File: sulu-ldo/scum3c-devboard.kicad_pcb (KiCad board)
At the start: 2 copper layers, 41.7 x 36.1 mm, 55 parts, among them J1 Conn_02x11_Odd_Even, J10 through_hole, J11 through_hole, J12 through_hole, J13 through_hole, J14 through_hole, J15 through_hole, J16 through_hole, J17 through_hole, J18 through_hole, J19 through_hole, J2 Conn_02x10_Odd_Even, J20 through_hole, J21 through_hole, J3 Conn_02x05_Odd_Even, J4 Conn_01x01_Male, J5 through_hole, J6 through_hole, J7 through_hole, J8 through_hole, J9 through_hole, U1 scum3, U2 S-85S1AB18-I6T1U, U3 S-85S1AB11-I6T1U, U9AB1 ICM-20948

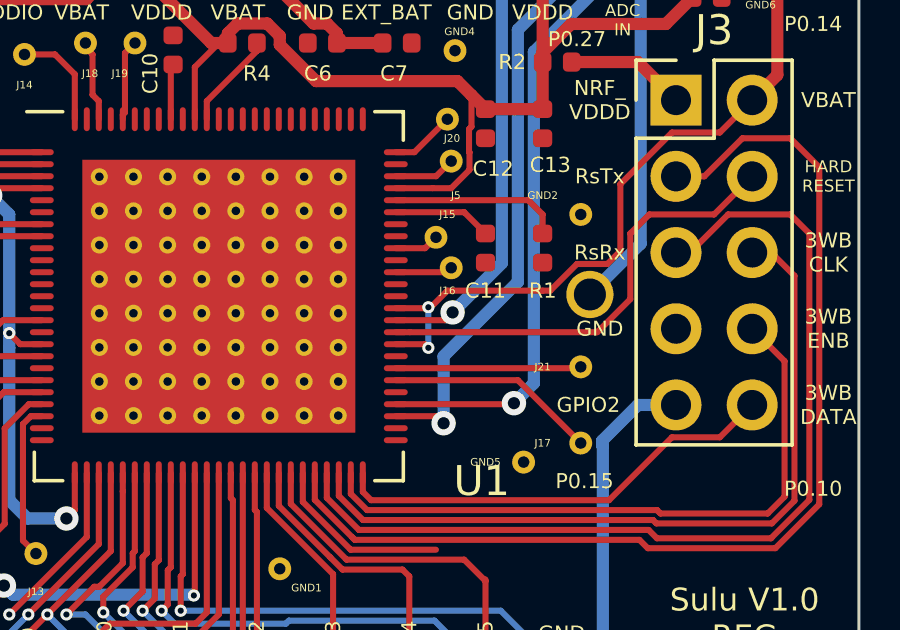
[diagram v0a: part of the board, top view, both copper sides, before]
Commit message: updated ldo with 3d model from reg
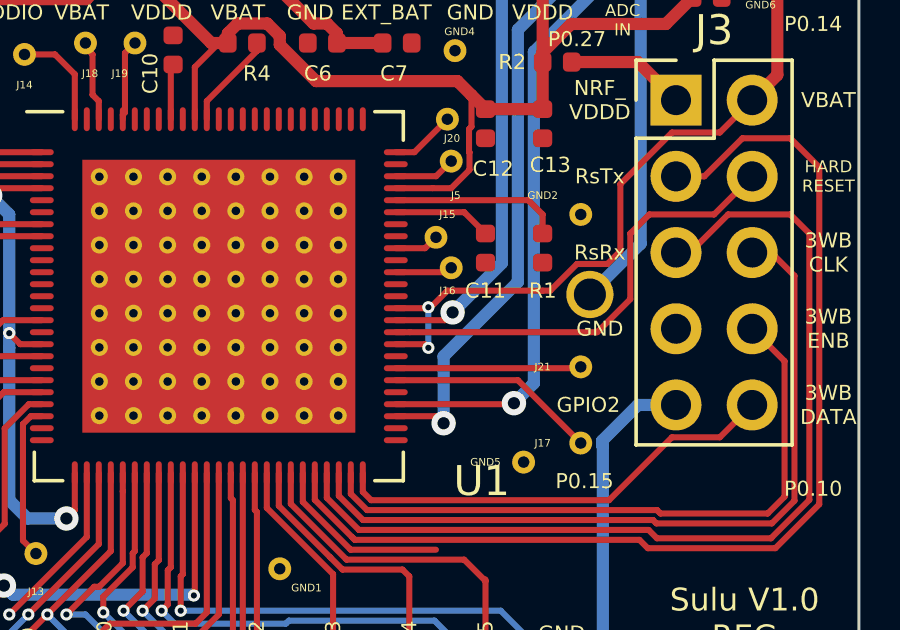
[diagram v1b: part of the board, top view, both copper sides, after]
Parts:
- removed BT1: BH1000G, downloaded_libs:BH1000G
- added B1: BH1000G, downloaded_libs:BH1000G, B.Cu at (124.7, 90.3)
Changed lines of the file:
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@@
     (thickness 1.6)
     (drawings 783)
-    (tracks 556)
+    (tracks 555)
     (zones 0)
     (modules 55)
@@
     (46 B.CrtYd user)
     (47 F.CrtYd user)
-    (48 B.Fab user hide)
-    (49 F.Fab user hide)
+    (48 B.Fab user)
+    (49 F.Fab user)
   )
   (setup
@@
     (uvia_drill 0.1)
   )
+  (module downloaded_libs:BH1000G (layer B.Cu)
+    (at 124.7394 90.297 270)
+    (fp_text reference B1 (at 0 -3.7465 270) (layer B.SilkS)
+      (effects (font (size 1 1) (thickness 0.15)) (justify mirror))
+    )
+    (fp_text value BH1000G (at 0 -3.7465 270) (layer B.SilkS)
+      (effects (font (size 1 1) (thickness 0.15)) (justify mirror))
+    )
+    (fp_text user * (at 0 0 270) (layer B.Fab)
+      (effects (font (size 1 1) (thickness 0.15)) (justify mirror))
+    )
+    (fp_text user * (at 0 0 270) (layer B.SilkS)
+      (effects (font (size 1 1) (thickness 0.15)) (justify mirror))
+    )
+    (fp_text user "Copyright 2021 Accelerated Designs. All rights reserved." (at 0 0 270) (layer Cmts.User)
+      (effects (font (size 0.127 0.127) (thickness 0.002)))
+    )
+    (fp_line (start -14.224 -15.3035) (end 14.224 -15.3035) (layer B.SilkS) (width 0.12))
+    (fp_line (start 14.224 -15.3035) (end 14.224 15.3035) (layer B.SilkS) (width 0.12))
+    (fp_line (start 14.224 15.3035) (end -14.224 15.3035) (layer B.SilkS) (width 0.12))
+    (fp_line (start -14.224 15.3035) (end -14.224 -15.3035) (layer B.SilkS) (width 0.12))
+    (fp_line (start -14.097 -15.1765) (end 14.097 -15.1765) (layer B.Fab) (width 0.1))
+    (fp_line (start 14.097 -15.1765) (end 14.097 15.1765) (layer B.Fab) (width 0.1))
+    (fp_line (start 14.097 15.1765) (end -14.097 15.1765) (layer B.Fab) (width 0.1))
+    (fp_line (start -14.097 15.1765) (end -14.097 -15.1765) (layer B.Fab) (width 0.1))
+    (fp_line (start -14.351 15.4305) (end -14.351 -15.4305) (layer B.CrtYd) (width 0.05))
+    (fp_line (start -14.351 -15.4305) (end 14.351 -15.4305) (layer B.CrtYd) (width 0.05))
+    (fp_line (start 14.351 -15.4305) (end 14.351 15.4305) (layer B.CrtYd) (width 0.05))
+    (fp_line (start 14.351 15.4305) (end -14.351 15.4305) (layer B.CrtYd) (width 0.05))
+    (fp_circle (center 0 8.4074) (end 0.381 8.4074) (layer B.Fab) (width 0.1))
+    (fp_circle (center -16.002 6.5024) (end -15.621 6.5024) (layer B.SilkS) (width 0.12))
+    (fp_circle (center -16.002 6.5024) (end -15.621 6.5024) (layer F.SilkS) (width 0.12))
+    (pad 2 thru_hole circle (at 0 -13.9954 270) (size 1.5748 1.5748) (drill 1.0668) (layers *.Cu *.Mask)
+      (net 57 +EXT_BAT))
+    (pad 1 thru_hole circle (at 0 6.5024 270) (size 1.5748 1.5748) (drill 1.0668) (layers *.Cu *.Mask)
+      (net 1 GND))
+    (model ${KIPRJMOD}/downloaded_libs/3D_Models/BH1000G.STEP
+      (at (xyz 0 0 0))
+      (scale (xyz 1 1 1))
+      (rotate (xyz -90 0 0))
+    )
+  )
   (module Connector_PinHeader_2.54mm:PinHeader_2x11_P2.54mm_Vertical (layer F.Cu)
     (at 114.3 78.74 90)
@@
     )
   )
-  (module downloaded_libs:BH1000G (layer B.Cu)
-    (at 124.7394 90.297 270)
-    (fp_text reference BT1 (at 0 -3.7465 90) (layer B.SilkS)
-      (effects (font (size 1 1) (thickness 0.15)) (justify mirror))
-    )
-    (fp_text value BH1000G (at 0 -3.7465 90) (layer B.SilkS)
-      (effects (font (size 1 1) (thickness 0.15)) (justify mirror))
-    )
-    (fp_circle (center -16.002 6.5024) (end -15.621 6.5024) (layer F.SilkS) (width 0.12))
-    (fp_circle (center -16.002 6.5024) (end -15.621 6.5024) (layer B.SilkS) (width 0.12))
-    (fp_circle (center 0 8.4074) (end 0.381 8.4074) (layer B.Fab) (width 0.1))
-    (fp_line (start 14.351 15.4305) (end -14.351 15.4305) (layer B.CrtYd) (width 0.05))
-    (fp_line (start 14.351 -15.4305) (end 14.351 15.4305) (layer B.CrtYd) (width 0.05))
-    (fp_line (start -14.351 -15.4305) (end 14.351 -15.4305) (layer B.CrtYd) (width 0.05))
-    (fp_line (start -14.351 15.4305) (end -14.351 -15.4305) (layer B.CrtYd) (width 0.05))
-    (fp_line (start -14.097 15.1765) (end -14.097 -15.1765) (layer B.Fab) (width 0.1))
-    (fp_line (start 14.097 15.1765) (end -14.097 15.1765) (layer B.Fab) (width 0.1))
-    (fp_line (start 14.097 -15.1765) (end 14.097 15.1765) (layer B.Fab) (width 0.1))
-    (fp_line (start -14.097 -15.1765) (end 14.097 -15.1765) (layer B.Fab) (width 0.1))
-    (fp_line (start -14.224 15.3035) (end -14.224 -15.3035) (layer B.SilkS) (width 0.12))
-    (fp_line (start 14.224 15.3035) (end -14.224 15.3035) (layer B.SilkS) (width 0.12))
-    (fp_line (start 14.224 -15.3035) (end 14.224 15.3035) (layer B.SilkS) (width 0.12))
-    (fp_line (start -14.224 -15.3035) (end 14.224 -15.3035) (layer B.SilkS) (width 0.12))
-    (fp_text user * (at 0 0 90) (layer B.Fab)
-      (effects (font (size 1 1) (thickness 0.15)) (justify mirror))
-    )
-    (fp_text user * (at 0 0 90) (layer B.SilkS)
-      (effects (font (size 1 1) (thickness 0.15)) (justify mirror))
-    )
-    (fp_text user "Copyright 2021 Accelerated Designs. All rights reserved." (at 0 0 90) (layer Cmts.User)
-      (effects (font (size 0.127 0.127) (thickness 0.002)))
-    )
-    (pad 2 thru_hole circle (at 0 -13.9954 270) (size 1.5748 1.5748) (drill 1.0668) (layers *.Cu *.Mask)
-      (net 57 +EXT_BAT))
-    (pad 1 thru_hole circle (at 0 6.5024 270) (size 1.5748 1.5748) (drill 1.0668) (layers *.Cu *.Mask)
-      (net 1 GND))
-  )
   (module Resistor_SMD:R_0402_1005Metric (layer F.Cu)
     (at 127.15 81.915)
@@
   (segment (start 125.593224 101.26979) (end 125.965 100.898014) (width 0.2032) (layer F.Cu) (net 24))
   (via (at 134.15814 90.894886) (size 0.8128) (drill 0.4064) (layers F.Cu B.Cu) (net 25))
-  (segment (start 133.985 91.068026) (end 134.15814 90.894886) (width 0.4064) (layer B.Cu) (net 25))
   (segment (start 133.898026 91.155) (end 134.15814 90.894886) (width 0.2032) (layer F.Cu) (net 25))
   (segment (start 132.265 91.155) (end 133.898026 91.155) (width 0.2032) (layer F.Cu) (net 25))

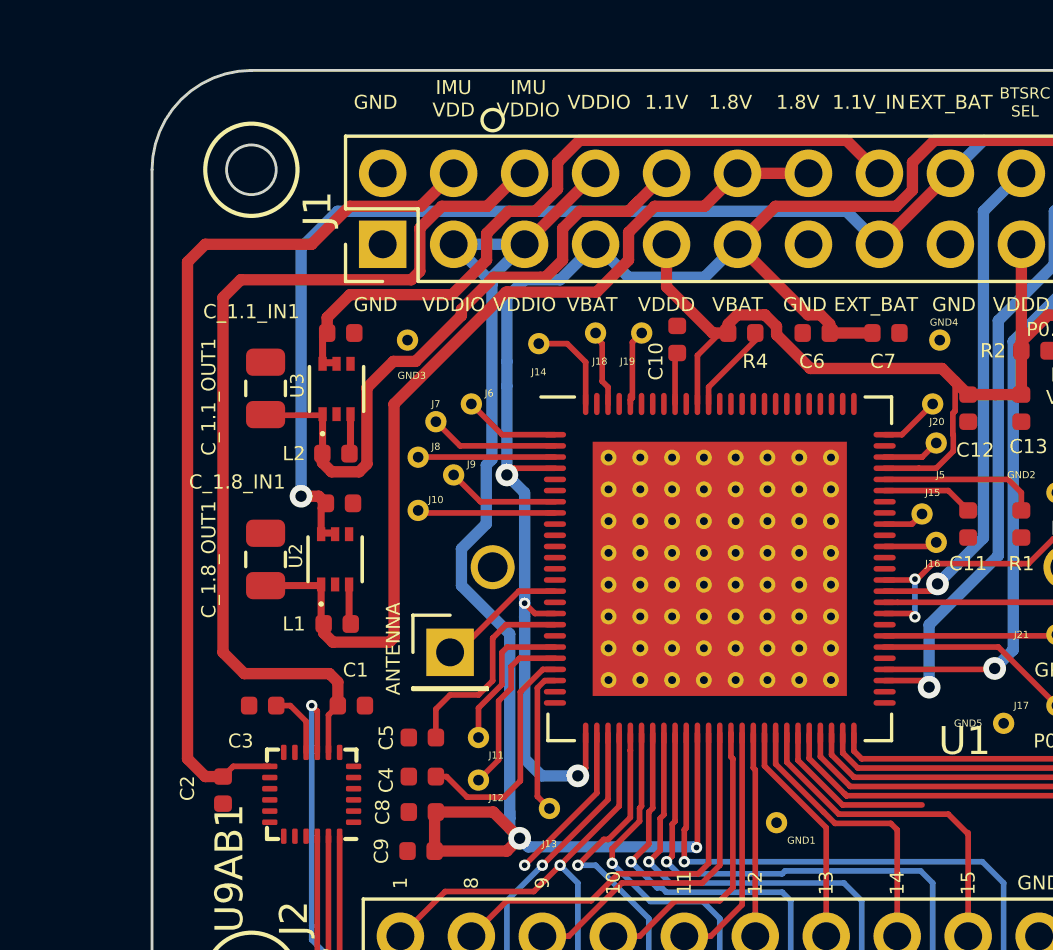
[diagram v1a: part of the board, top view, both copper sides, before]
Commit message: connected ldo traces
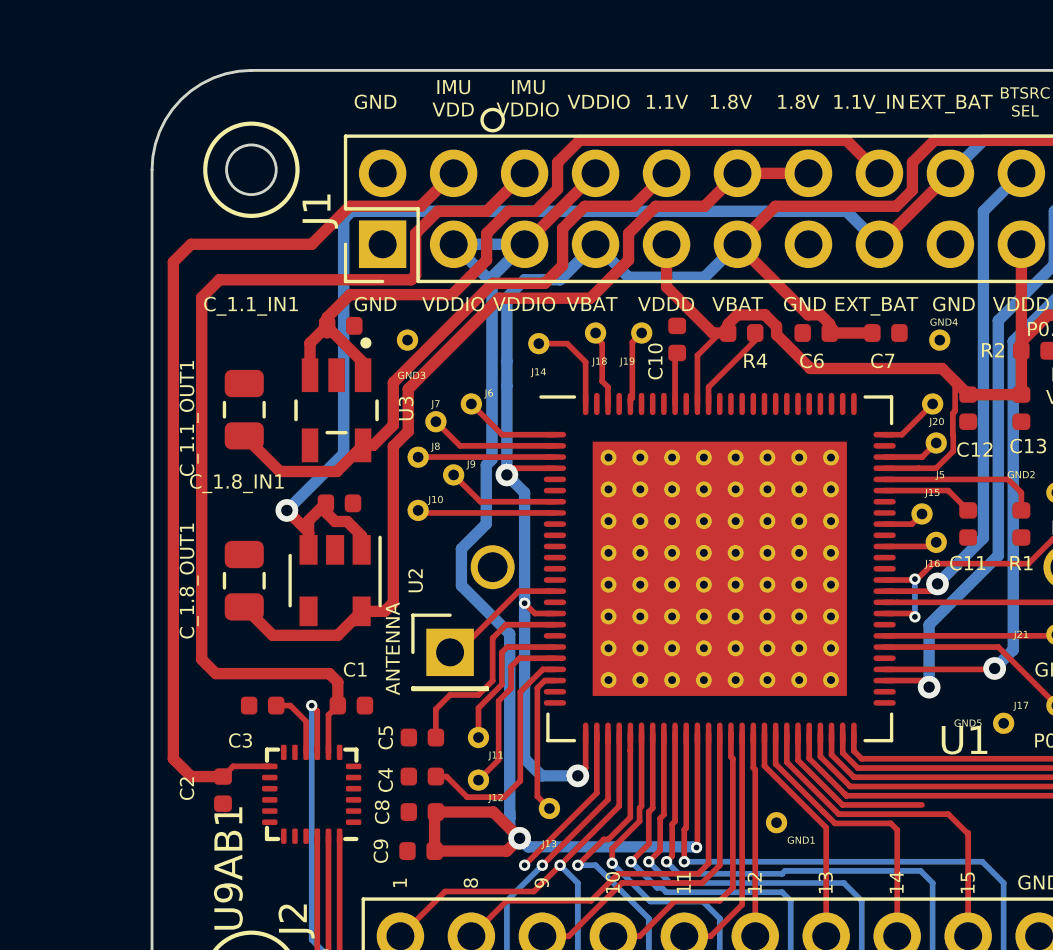
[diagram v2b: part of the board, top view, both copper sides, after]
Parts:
- removed L1, L2: 2.2 uH, Inductor_SMD:L_0402_1005Metric
- U2: value S-85S1AB18-I6T1U -> LP5907MFX-1.8; footprint downloaded_libs:SOFL50P180X50-6N -> Package_TO_SOT_SMD:SOT-23-5
- U3: value S-85S1AB11-I6T1U -> TLV70311DBVR; footprint downloaded_libs:SOFL50P180X50-6N -> downloaded_libs:SOT95P280X145-5N
- moved C_1.1_OUT1 1.08 mm to (109.3, 84.7)
- moved C_1.8_OUT1 1.08 mm to (109.3, 90.8)
- moved U2 0.76 mm to (112.6, 90.8), turned to 270 degrees
- moved U3 0.76 mm to (112.6, 84.7), turned to 270 degrees
- moved C_1.1_IN1 0.25 mm to (112.8, 81.7)
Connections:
- U2 pad 1: +1.8V_REG -> +EXT_BAT
- U2 pad 3: Net-(L1-Pad2) -> +EXT_BAT
- U2 pad 4: GND -> (no net)
- U2 pad 5: +EXT_BAT -> +1.8V_REG
- U3 pad 1: +1.1V_REG -> /1.1V_IN
- U3 pad 3: Net-(L2-Pad2) -> /1.1V_IN
- U3 pad 4: GND -> (no net)
- U3 pad 5: /1.1V_IN -> +1.1V_REG
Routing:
- net +EXT_BAT: track 59.4 -> 63.3 mm
- net /1.1V_IN: track 26.2 -> 28.9 mm
- net /IMU_VDDIO: track 34.1 -> 35.9 mm
- net +1.8V_REG: track 33.9 -> 32.2 mm
- net +1.1V_REG: track 24.1 -> 22.5 mm
- net Net-(L1-Pad2): track 1.44 -> 0.00 mm
- net Net-(L2-Pad2): track 1.13 -> 0.00 mm
- net /IMU_VDD: track 32.0 -> 33.0 mm
